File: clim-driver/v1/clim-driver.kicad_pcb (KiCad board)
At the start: 2 copper layers, 60 x 40 mm, 14 parts, among them J1 Conn_01x03_Male, J2 Screw_Terminal_01x02, J3 Conn_01x02_Pin, Q1 BSS138, U1 WeMos_D1_mini

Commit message: wip pcb
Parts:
- moved D1 119.5 mm to (101.9, 104.8)
- moved R1 119.5 mm to (105.6, 104.2)
- moved R2 119.5 mm to (101.7, 107.5)
- moved Q1 89.7 mm to (110.6, 106.6)
- moved R3 89.7 mm to (110.9, 102.2)
- moved J1 86.5 mm to (120.7, 66.7), turned to 180 degrees
- moved J3 84.6 mm to (120.7, 73.0)
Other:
- board text added: "+"
- board text added: "-"
- board text added: "3V3"
- board text added: "DS18B20"
- board text added: "GND"
- board text added: "IN"
- board text added: "LED IR"
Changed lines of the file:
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@@
   )
   (footprint "Resistor_SMD:R_0603_1608Metric" (layer "F.Cu")
-    (at 1.505 42.345)
+    (at 101.6925 107.55)
     (descr "Resistor SMD 0603 (1608 Metric), square (rectangular) end terminal, IPC_7351 nominal, (Body size source: IPC-SM-782 page 72, https://www.pcb-3d.com/wordpress/wp-content/uploads/ipc-sm-782a_amendment_1_and_2.pdf), generated with kicad-footprint-generator")
     (tags "resistor")
@@
   )
   (footprint "Connector_PinHeader_2.54mm:PinHeader_1x03_P2.54mm_Vertical" (layer "F.Cu")
-    (at 39.205 37.575)
+    (at 120.65 66.675 180)
     (descr "Through hole straight pin header, 1x03, 2.54mm pitch, single row")
     (tags "Through hole pin header THT 1x03 2.54mm single row")
@@
     (property "ki_keywords" "connector")
     (attr through_hole)
-    (fp_text reference "J1" (at 0 -2.33) (layer "F.SilkS")
+    (fp_text reference "J1" (at 3.175 3.175) (layer "F.SilkS")
         (effects (font (size 1 1) (thickness 0.15)))
     )
@@
     (fp_line (start 1.27 6.35) (end -1.27 6.35)
       (stroke (width 0.1) (type solid)) (layer "F.Fab"))
-    (pad "1" thru_hole rect (at 0 0) (size 1.7 1.7) (drill 1) (layers "*.Cu" "*.Mask")
+    (pad "1" thru_hole rect (at 0 0 180) (size 1.7 1.7) (drill 1) (layers "*.Cu" "*.Mask")
       (net 1 "GND") (pinfunction "Pin_1") (pintype "passive"))
-    (pad "2" thru_hole oval (at 0 2.54) (size 1.7 1.7) (drill 1) (layers "*.Cu" "*.Mask")
+    (pad "2" thru_hole oval (at 0 2.54 180) (size 1.7 1.7) (drill 1) (layers "*.Cu" "*.Mask")
       (net 3 "+3V3") (pinfunction "Pin_2") (pintype "passive"))
-    (pad "3" thru_hole oval (at 0 5.08) (size 1.7 1.7) (drill 1) (layers "*.Cu" "*.Mask")
+    (pad "3" thru_hole oval (at 0 5.08 180) (size 1.7 1.7) (drill 1) (layers "*.Cu" "*.Mask")
       (net 9 "Net-(J1-Pin_3)") (pinfunction "Pin_3") (pintype "passive"))
     (model "${KICAD6_3DMODEL_DIR}/Connector_PinHeader_2.54mm.3dshapes/PinHeader_1x03_P2.54mm_Vertical.wrl"
@@
   )
   (footprint "Package_TO_SOT_SMD:SOT-23" (layer "F.Cu")
-    (at 48.625 41.685)
+    (at 110.5725 106.565)
     (descr "SOT, 3 Pin (https://www.jedec.org/system/files/docs/to-236h.pdf variant AB), generated with kicad-footprint-generator ipc_gullwing_generator.py")
     (tags "SOT TO_SOT_SMD")
@@
   )
   (footprint "Diode_SMD:D_0805_2012Metric" (layer "F.Cu")
-    (at 1.745 39.57)
+    (at 101.9325 104.775)
     (descr "Diode SMD 0805 (2012 Metric), square (rectangular) end terminal, IPC_7351 nominal, (Body size source: https://docs.google.com/spreadsheets/d/1BsfQQcO9C6DZCsRaXUlFlo91Tg2WpOkGARC1WS5S8t0/edit?usp=sharing), generated with kicad-footprint-generator")
     (tags "diode")
@@
   )
   (footprint "Resistor_SMD:R_1210_3225Metric" (layer "F.Cu")
-    (at 48.985 37.355)
+    (at 110.9325 102.235)
     (descr "Resistor SMD 1210 (3225 Metric), square (rectangular) end terminal, IPC_7351 nominal, (Body size source: IPC-SM-782 page 72, https://www.pcb-3d.com/wordpress/wp-content/uploads/ipc-sm-782a_amendment_1_and_2.pdf), generated with kicad-footprint-generator")
     (tags "resistor")
@@
   )
   (footprint "Connector_PinHeader_2.54mm:PinHeader_1x02_P2.54mm_Vertical" (layer "F.Cu")
-    (at 43.855 37.575)
+    (at 120.65 73.025)
     (descr "Through hole straight pin header, 1x02, 2.54mm pitch, single row")
     (tags "Through hole pin header THT 1x02 2.54mm single row")
@@
     (property "ki_keywords" "connector")
     (attr through_hole)
-    (fp_text reference "J3" (at 0 -2.33) (layer "F.SilkS")
+    (fp_text reference "J3" (at -3.175 0.635) (layer "F.SilkS")
         (effects (font (size 1 1) (thickness 0.15)))
     )
@@
   )
   (footprint "Resistor_SMD:R_0402_1005Metric" (layer "F.Cu")
-    (at 5.405 39.045)
+    (at 105.5925 104.25)
     (descr "Resistor SMD 0402 (1005 Metric), square (rectangular) end terminal, IPC_7351 nominal, (Body size source: IPC-SM-782 page 72, https://www.pcb-3d.com/wordpress/wp-content/uploads/ipc-sm-782a_amendment_1_and_2.pdf), generated with kicad-footprint-generator")
     (tags "resistor")
@@
   (gr_rect locked (start 90 46) (end 150 86)
     (stroke (width 0.1) (type default)) (fill none) (layer "Edge.Cuts"))
+  (gr_text "DS18B20" (at 117.475 59.69) (layer "F.SilkS")
+    (effects (font (size 1 1) (thickness 0.15)) (justify left bottom))
+  )
+  (gr_text "-" (at 123.825 75.565) (layer "F.SilkS")
+    (effects (font (size 0.6 0.6) (thickness 0.125)))
+  )
+  (gr_text "GND" (at 123.825 66.675) (layer "F.SilkS")
+    (effects (font (size 0.6 0.6) (thickness 0.125)))
+  )
+  (gr_text "3V3" (at 123.825 64.135) (layer "F.SilkS")
+    (effects (font (size 0.6 0.6) (thickness 0.125)))
+  )
+  (gr_text "LED IR" (at 118.11 71.12) (layer "F.SilkS")
+    (effects (font (size 1 1) (thickness 0.15)) (justify left bottom))
+  )
+  (gr_text "+" (at 123.825 73.025) (layer "F.SilkS")
+    (effects (font (size 0.6 0.6) (thickness 0.125)))
+  )
+  (gr_text "IN" (at 123.825 61.595) (layer "F.SilkS")
+    (effects (font (size 0.6 0.6) (thickness 0.125)))
+  )
   (group "" locked (id d43d666a-10bd-47fa-a783-07e68fd1da55)
     (members

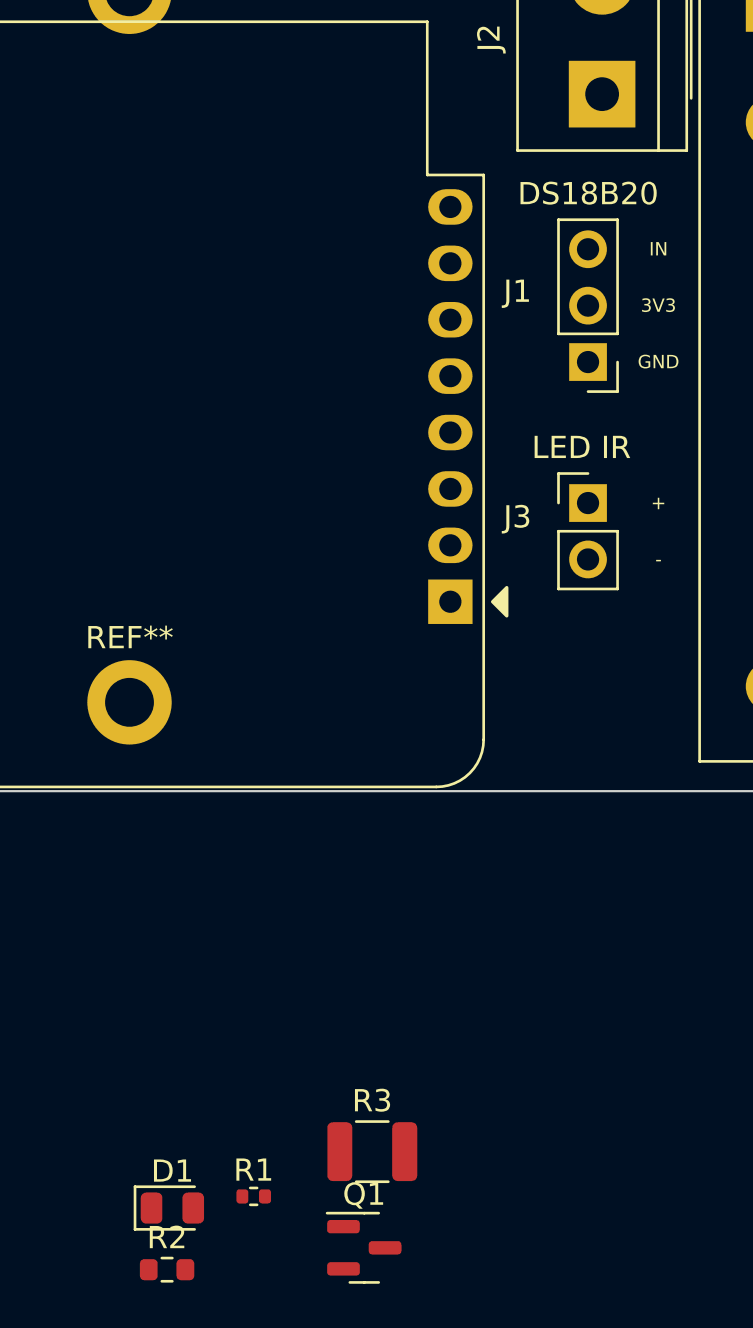
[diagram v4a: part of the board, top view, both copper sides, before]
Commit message: pcb placement
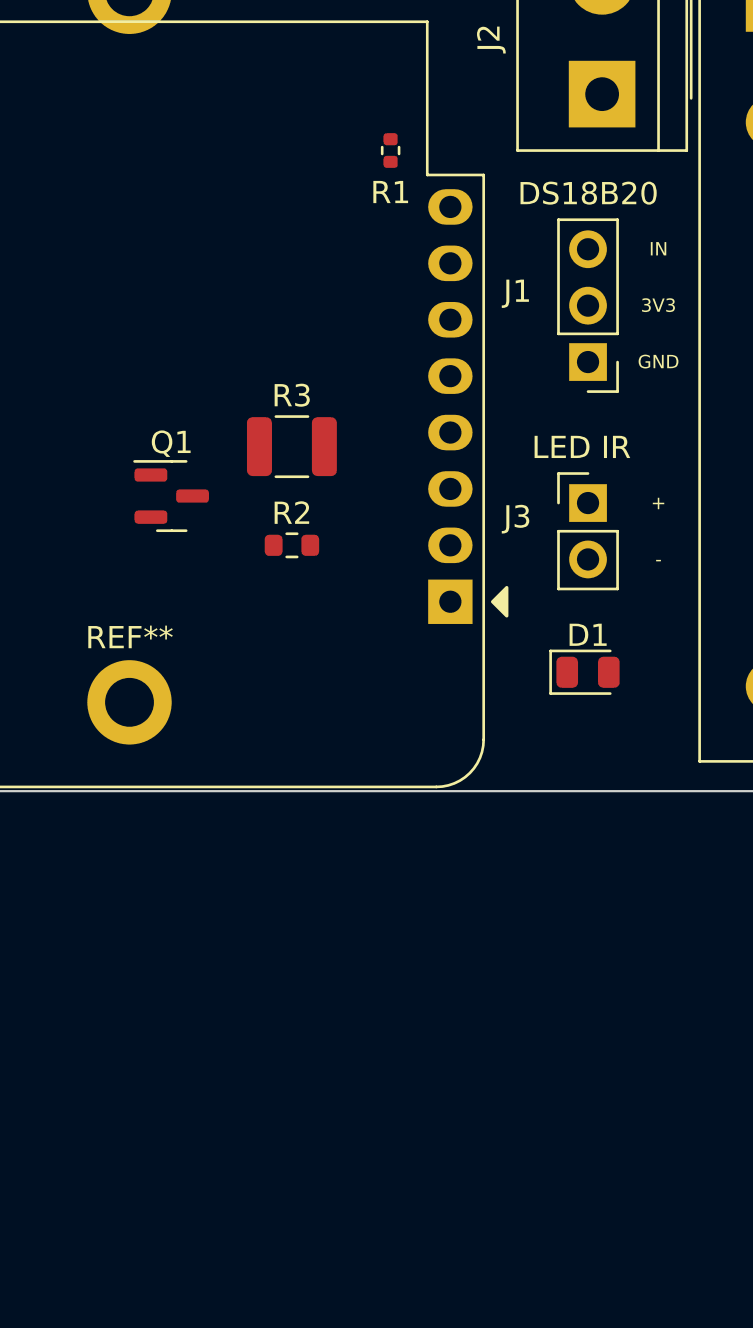
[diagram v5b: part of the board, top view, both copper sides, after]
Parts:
- moved R1 47.5 mm to (111.8, 57.1), turned to 90 degrees
- moved Q1 34.9 mm to (101.9, 72.7)
- moved R2 33.1 mm to (107.3, 74.9)
- moved R3 32.0 mm to (107.3, 70.5)
- moved D1 30.5 mm to (120.7, 80.6)
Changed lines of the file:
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@@
   )
   (footprint "Resistor_SMD:R_0603_1608Metric" (layer "F.Cu")
-    (at 101.6925 107.55)
+    (at 107.315 74.93)
     (descr "Resistor SMD 0603 (1608 Metric), square (rectangular) end terminal, IPC_7351 nominal, (Body size source: IPC-SM-782 page 72, https://www.pcb-3d.com/wordpress/wp-content/uploads/ipc-sm-782a_amendment_1_and_2.pdf), generated with kicad-footprint-generator")
     (tags "resistor")
@@
   )
   (footprint "Package_TO_SOT_SMD:SOT-23" (layer "F.Cu")
-    (at 110.5725 106.565)
+    (at 101.9025 72.71)
     (descr "SOT, 3 Pin (https://www.jedec.org/system/files/docs/to-236h.pdf variant AB), generated with kicad-footprint-generator ipc_gullwing_generator.py")
     (tags "SOT TO_SOT_SMD")
@@
   )
   (footprint "Diode_SMD:D_0805_2012Metric" (layer "F.Cu")
-    (at 101.9325 104.775)
+    (at 120.65 80.645)
     (descr "Diode SMD 0805 (2012 Metric), square (rectangular) end terminal, IPC_7351 nominal, (Body size source: https://docs.google.com/spreadsheets/d/1BsfQQcO9C6DZCsRaXUlFlo91Tg2WpOkGARC1WS5S8t0/edit?usp=sharing), generated with kicad-footprint-generator")
     (tags "diode")
@@
   )
   (footprint "Resistor_SMD:R_1210_3225Metric" (layer "F.Cu")
-    (at 110.9325 102.235)
+    (at 107.315 70.485)
     (descr "Resistor SMD 1210 (3225 Metric), square (rectangular) end terminal, IPC_7351 nominal, (Body size source: IPC-SM-782 page 72, https://www.pcb-3d.com/wordpress/wp-content/uploads/ipc-sm-782a_amendment_1_and_2.pdf), generated with kicad-footprint-generator")
     (tags "resistor")
@@
   )
   (footprint "Resistor_SMD:R_0402_1005Metric" (layer "F.Cu")
-    (at 105.5925 104.25)
+    (at 111.76 57.15 90)
     (descr "Resistor SMD 0402 (1005 Metric), square (rectangular) end terminal, IPC_7351 nominal, (Body size source: IPC-SM-782 page 72, https://www.pcb-3d.com/wordpress/wp-content/uploads/ipc-sm-782a_amendment_1_and_2.pdf), generated with kicad-footprint-generator")
     (tags "resistor")
@@
     (property "ki_keywords" "R res resistor")
     (attr smd)
-    (fp_text reference "R1" (at 0 -1.17) (layer "F.SilkS")
-        (effects (font (size 1 1) (thickness 0.15)))
-    )
-    (fp_text value "4.7KΩ" (at 0 1.17) (layer "F.Fab")
-        (effects (font (size 1 1) (thickness 0.15)))
-    )
-    (fp_text user "${REFERENCE}" (at 0 0) (layer "F.Fab")
+    (fp_text reference "R1" (at -1.905 0) (layer "F.SilkS")
+        (effects (font (size 1 1) (thickness 0.15)))
+    )
+    (fp_text value "4.7KΩ" (at 0 1.17 90) (layer "F.Fab")
+        (effects (font (size 1 1) (thickness 0.15)))
+    )
+    (fp_text user "${REFERENCE}" (at 0 0 90) (layer "F.Fab")
         (effects (font (size 0.26 0.26) (thickness 0.04)))
     )
@@
     (fp_line (start 0.525 0.27) (end -0.525 0.27)
       (stroke (width 0.1) (type solid)) (layer "F.Fab"))
-    (pad "1" smd roundrect (at -0.51 0) (size 0.54 0.64) (layers "F.Cu" "F.Paste" "F.Mask") (roundrect_rratio 0.25)
+    (pad "1" smd roundrect (at -0.51 0 90) (size 0.54 0.64) (layers "F.Cu" "F.Paste" "F.Mask") (roundrect_rratio 0.25)
       (net 3 "+3V3") (pintype "passive"))
-    (pad "2" smd roundrect (at 0.51 0) (size 0.54 0.64) (layers "F.Cu" "F.Paste" "F.Mask") (roundrect_rratio 0.25)
+    (pad "2" smd roundrect (at 0.51 0 90) (size 0.54 0.64) (layers "F.Cu" "F.Paste" "F.Mask") (roundrect_rratio 0.25)
       (net 9 "Net-(J1-Pin_3)") (pintype "passive"))
     (model "${KICAD6_3DMODEL_DIR}/Resistor_SMD.3dshapes/R_0402_1005Metric.wrl"
